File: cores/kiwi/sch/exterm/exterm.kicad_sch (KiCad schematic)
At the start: 6 parts, among them J1 R_Pack08, J2 R_P, J5 R_P

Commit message: Schematics PDF moved to JTBIN
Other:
- sheet mcu ports: added ~{MCU_RST}; removed ~{RST}
- sheet sound ports: added ~{MCU_RST}; removed ~{RST}
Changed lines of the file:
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@@
     (effects (font (size 1.27 1.27)) (justify right bottom))
   )
-  (label "~{RST}" (at 215.9 49.53 0)
+  (label "~{MCU_RST}" (at 215.9 49.53 0)
     (effects (font (size 1.27 1.27)) (justify left bottom))
   )
@@
     (effects (font (size 1.27 1.27)) (justify left bottom))
   )
-  (label "~{RST}" (at 276.86 128.27 180)
+  (label "~{MCU_RST}" (at 276.86 128.27 180)
     (effects (font (size 1.27 1.27)) (justify right bottom))
   )
@@
       (effects (font (size 1.27 1.27)) (justify left))
     )
-    (pin "~{RST}" input (at 229.87 49.53 180)
+    (pin "~{MCU_RST}" input (at 229.87 49.53 180)
       (effects (font (size 1.27 1.27)) (justify left))
     )
@@
       (effects (font (size 1.27 1.27)) (justify right))
     )
-    (pin "~{RST}" output (at 261.62 128.27 0)
-      (effects (font (size 1.27 1.27)) (justify right))
-    )
+    (pin "~{MCU_RST}" output (at 261.62 128.27 0)
+      (effects (font (size 1.27 1.27)) (justify right))
+    )

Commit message: issue#46
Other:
- sheet colmix ports: added H1_BUF; removed H1B
- sheet gfx ports: added GFX_~{CE}, H3_BUF, H4_BUF, VBLK, ~{OBJCODELO}; removed H3B, H4B, MAB_~{CE}, MBB_~{CE}, ~{MAIN_WR}, ~{VBLK}, ~{WR}
- sheet main ports: added GFX_~{CE}, H0_BUF, H1_BUF, H2_BUF, H3_BUF, H4_BUF, MAIN_VD[15..8], VBLK, WATCHDOG, ~{OBJCODELO}, ~{SBNKMWR}, ~{SBNKSWR}; removed CLK_SND, H1B, H3B, H4B, MAB_~{CE}, MBB_~{CE}, PHM, SHD[7..0], SND_D[7..0], SND_~{INT}, S_~{IORQ}, YM_~{CS}, ~{MAIN_WR}, ~{VBLK}, ~{WATCHDOG}, ~{WR}
- sheet mcu ports: added H1_BUF; removed H1B
- sheet sound ports: added H0_BUF, H2_BUF, MAIN_VD[15..8], ~{SBNKMWR}, ~{SBNKSWR}; removed CLK_SND, PHM, SHD[7..0], SND_~{INT}, S_~{IORQ}, YM_~{CS}
- sheet watchdog ports: added WATCHDOG; removed ~{WATCHDOG}

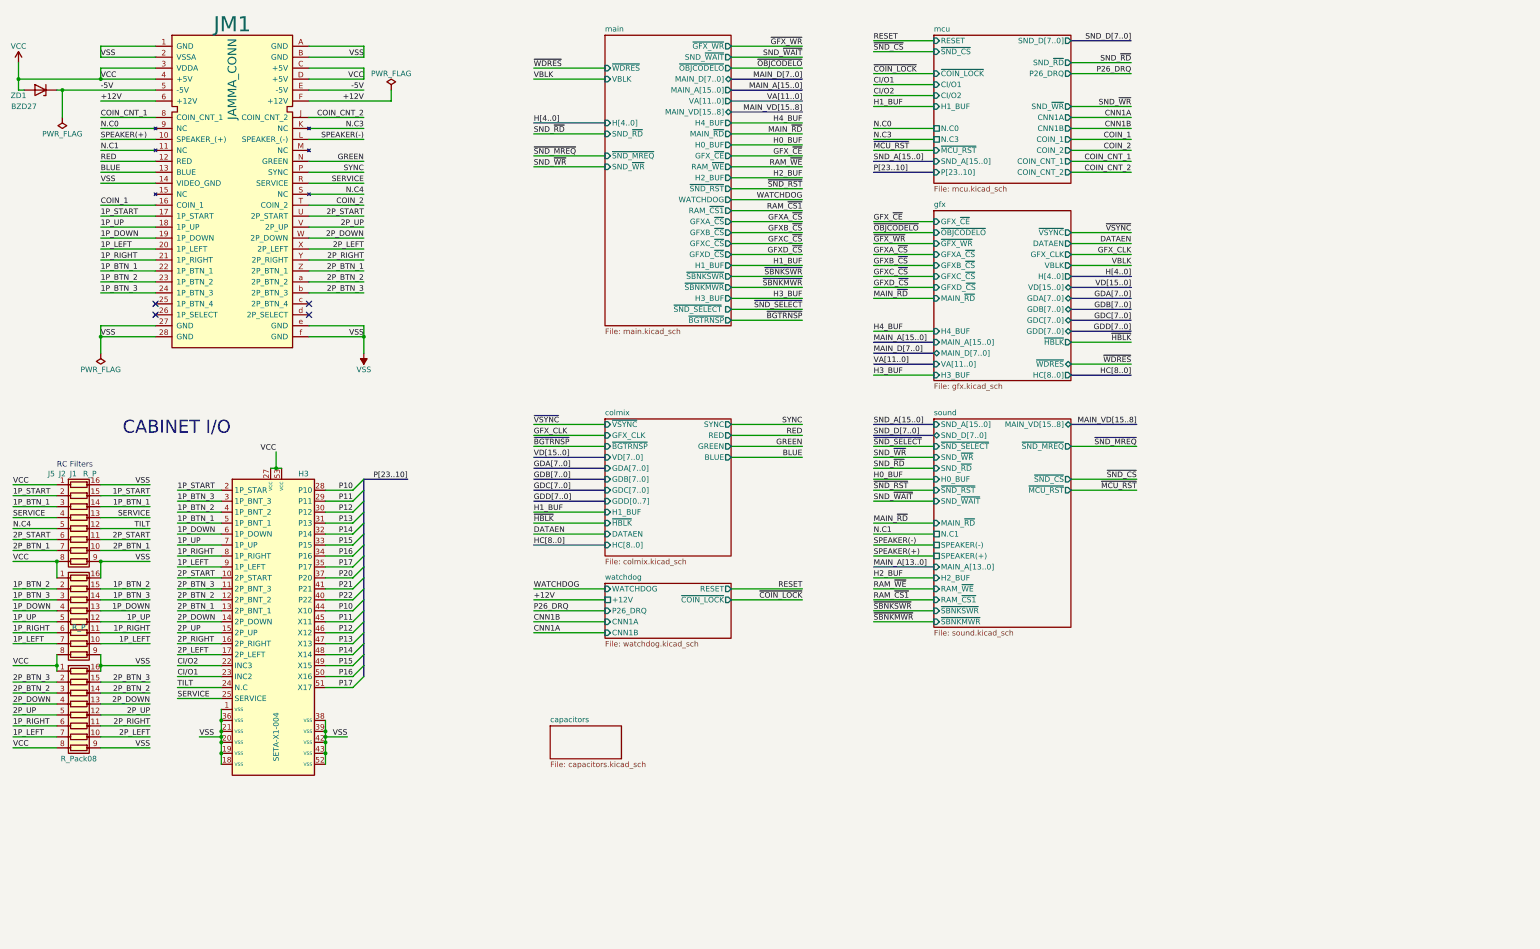
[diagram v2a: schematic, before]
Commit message: sheet_size_update
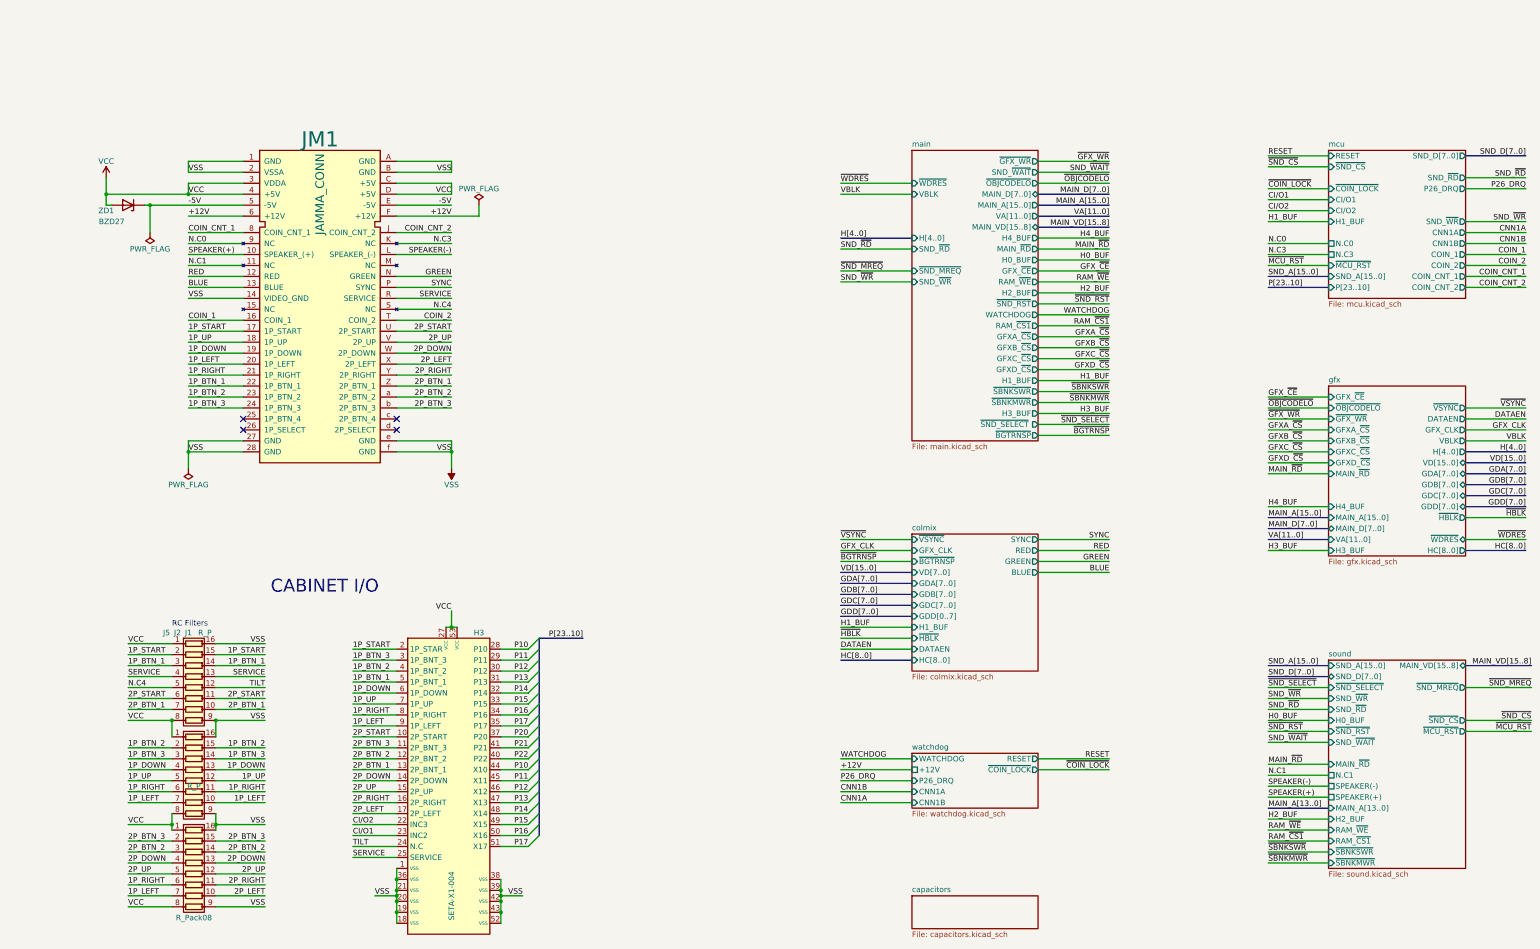
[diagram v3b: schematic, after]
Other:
- moved on the sheet: H3, J1, J2, J5, JM1, ZD1
